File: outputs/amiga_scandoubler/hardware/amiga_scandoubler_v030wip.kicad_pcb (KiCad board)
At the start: 4 copper layers, 95 x 95 mm, 135 parts, among them J1 33DSMT1-E15SNCT, J2 33DSMT1-E15SNCT, J3 TYPE-C-31-M-12, J4 JTAG 2x05 2.54mm, U1 TVP7002PZP, U2 GW1N-LV4QN88C6/I5, U3 ADV7125KSTZ140, U4 SN74LVC2G17DBVR, U5 SN74LVC2G17DBVR, U6 SN74LVC1G17DBVR, U7 TPS62160DSGR, U8 TPS62160DSGR, U9 TPS62160DSGR, Y1 27MHz ECS-3225MVLC

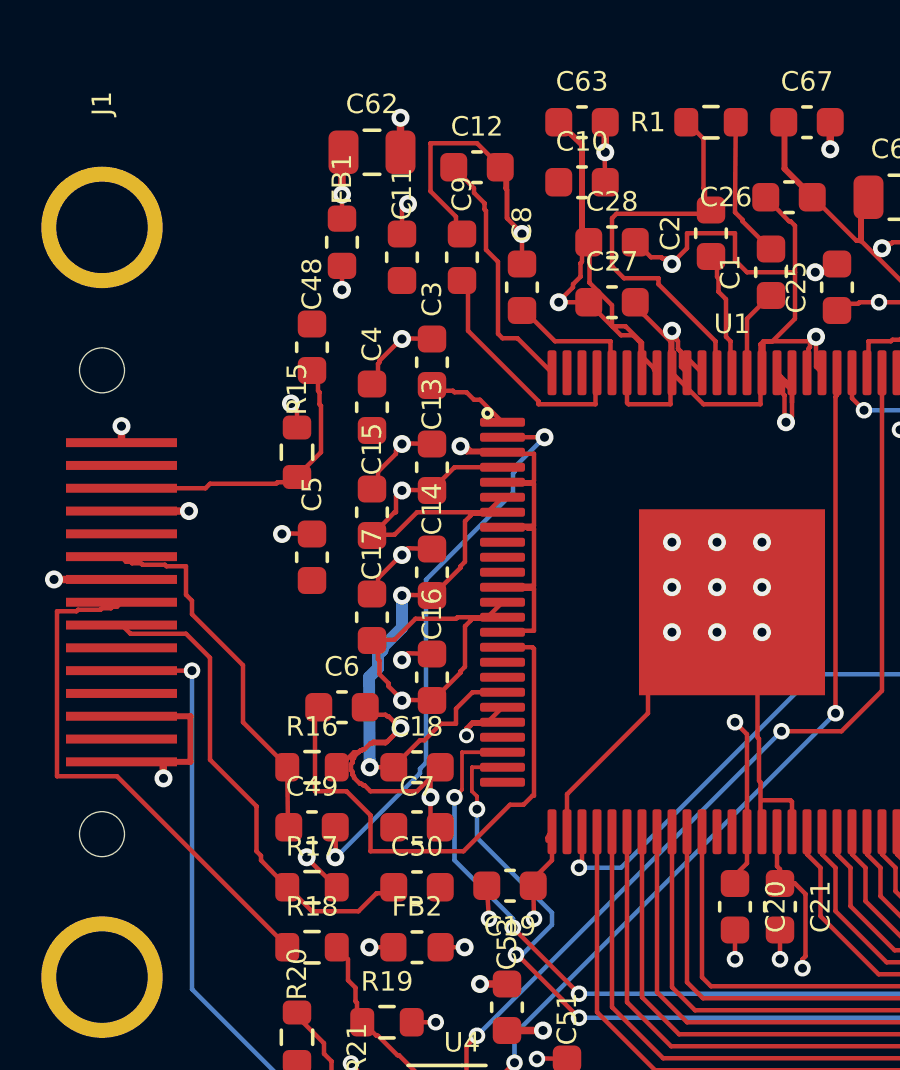
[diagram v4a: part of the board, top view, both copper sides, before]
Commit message: Issue 8: route the last analog inputs (board fully connected)
- Open the U1 input pins that other routing had walled in:
  - ADC_1V9A pin7 -> C14 and ADC_3V3A pin13/14 -> C16. The caps stay connected through their vias and In2.
  - The GIN_4, BIN_3 and GIN_1 routes.
  - The In2 ADC_1V9A and ADC_3V3A lines.
- RIN_1-3 escape through vias west of pins 9-11. The rest were routed with router7 and saved in p8_routes.json.
- The In2 3V3 zone now always removes isolated fill islands.
- DRC errors 0. Unconnected items 7 -> 0. 28 connectivity pairs checked. The power audit is unchanged.

Co-Authored-By: Claude Opus 5.5 <noreply@anthropic.com>
Claude-Session: https://claude.ai/code/session_019f929sAJ7LRnJRRFvA6g9F
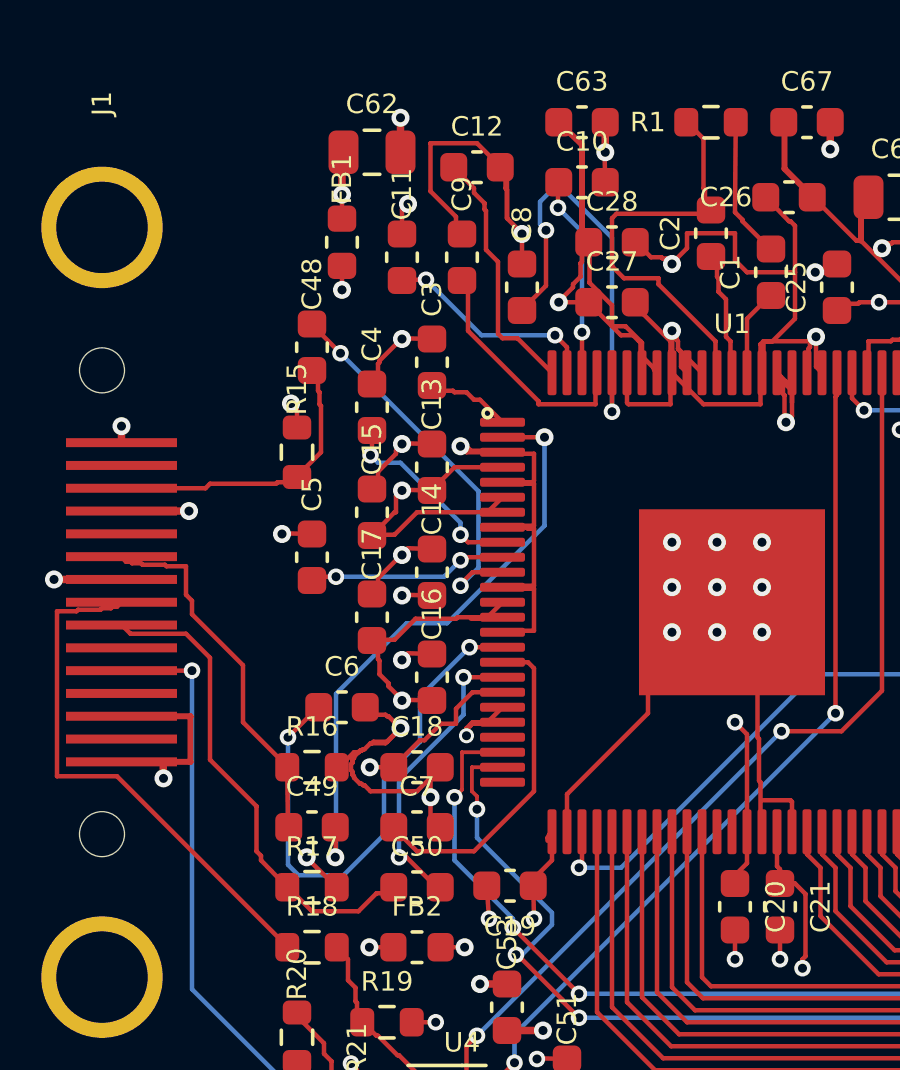
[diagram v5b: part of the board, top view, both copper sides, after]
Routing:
- net RIN_1: track 0.00 -> 12.1 mm, vias 0 -> 2
- net BIN_2: track 0.00 -> 11.1 mm
- net BIN_1: track 0.00 -> 9.95 mm, vias 0 -> 2
- net GIN_4: track 4.48 -> 14.3 mm, vias 0 -> 2
- net SOGIN_2: track 0.00 -> 7.28 mm, vias 0 -> 2
- net GIN_3: track 0.00 -> 6.68 mm, vias 0 -> 2
- net RIN_3: track 0.00 -> 5.96 mm, vias 0 -> 2
- net RIN_2: track 0.00 -> 5.91 mm, vias 0 -> 2
- net ADC_1V9A: track 63.0 -> 59.1 mm
- net ADC_3V3A: track 55.7 -> 53.6 mm
- net GIN_1: track 19.3 -> 20.1 mm
- net BIN_3: track 18.4 -> 18.1 mm, vias 0 -> 2

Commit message: Review fixes: decaps for U2 VCCO pins 12/23; move In2 lines off GIN_1
- #1: Add C70/C71 (100nF 0402) at 1.5 / 1.1 mm from U2 pins 12/23. Schematic, netlist and manifest updated; the schematic export matches the board on 591 nodes.
- #2: Re-draw the In2 ADC_3V3A/ADC_1V9A links so they cross GIN_1 instead of running under it (gap 4.9 -> 4.5 mm).
- #3: Stitching vias dropped. With In1 as the only GND plane they connect to nothing. Decaps near the REF_27M vias remain proposed.
- DRC errors 0, unconnected 0. The audit passes; its part/pad counts are updated to 137/596.

Co-Authored-By: Claude Opus 5.5 <noreply@anthropic.com>
Claude-Session: https://claude.ai/code/session_019f929sAJ7LRnJRRFvA6g9F
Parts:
- added C70: 100nF, C_0402_1005Metric, F.Cu at (57.0, 42.0)
- added C71: 100nF, C_0402_1005Metric, F.Cu at (54.8, 35.9)
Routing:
- net GND: track 370.1 -> 371.2 mm, vias 126 -> 127
- net 3V3: track 82.8 -> 83.5 mm
- net ADC_1V9A: track 59.1 -> 59.7 mm

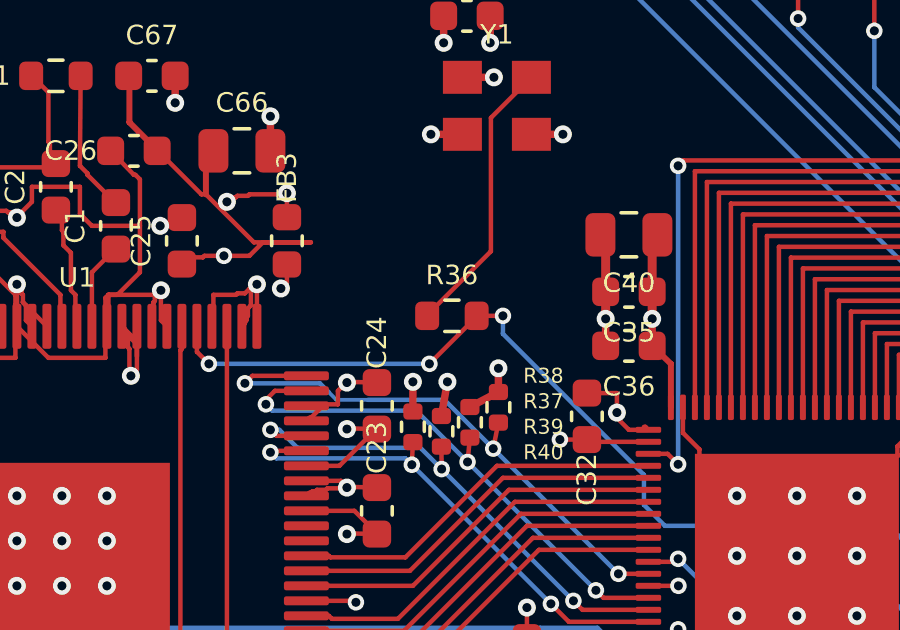
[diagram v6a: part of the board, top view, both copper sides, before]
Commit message: Add decaps C72/C73 next to the REF_27M layer-change vias
- Placements found by tools/capvia.py (0402, short stubs to new plane vias, no via-in-pad).
- Via-to-decap distance: 5.2 -> 1.6 mm and 4.3 -> 0.8 mm. The via under U1 (30.4,35.6) has no room and stays at 6.2 mm.
- Schematic (02_fpga), netlist and manifest updated; the schematic export matches the board on 595 nodes.
- DRC errors 0, unconnected 0. The audit passes with 139 parts / 600 pad nets.

Co-Authored-By: Claude Opus 5.5 <noreply@anthropic.com>
Claude-Session: https://claude.ai/code/session_019f929sAJ7LRnJRRFvA6g9F
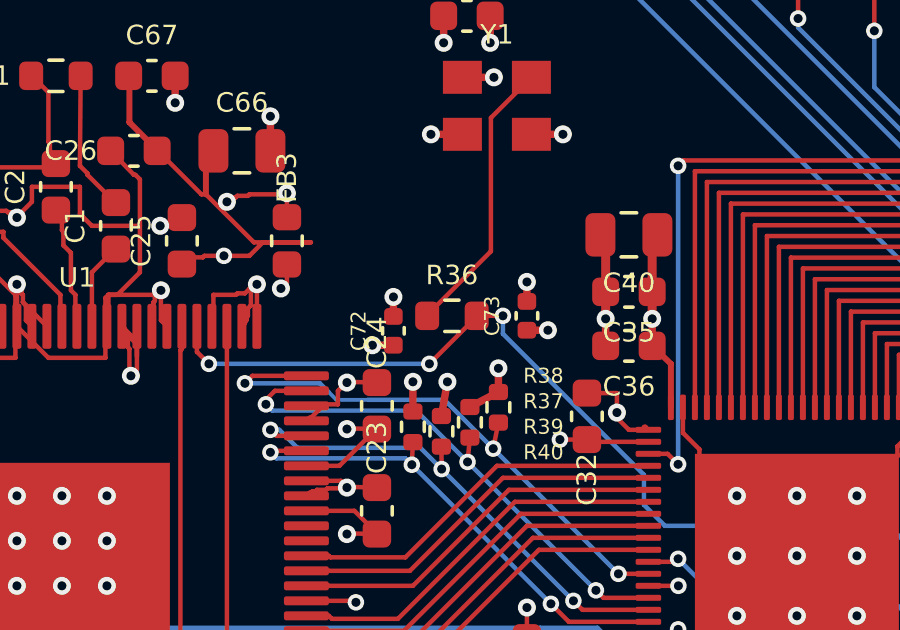
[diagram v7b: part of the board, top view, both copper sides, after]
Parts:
- added C72: 100nF, C_0402_1005Metric, F.Cu at (36.5, 34.5)
- added C73: 100nF, C_0402_1005Metric, F.Cu at (41.0, 34.0)
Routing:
- net 3V3: track 83.5 -> 84.9 mm, vias 39 -> 41
- net GND: track 371.2 -> 372.5 mm, vias 127 -> 129
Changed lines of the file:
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@@
     )
   )
+  (footprint "C_0402_1005Metric" (layer "F.Cu")
+    (at 36.55 34.5 90)
+    (descr "Capacitor SMD 0402 (1005 Metric), square (rectangular) end terminal, IPC_7351 nominal, (Body size source: IPC-SM-782 page 76, https://www.pcb-3d.com/wordpress/wp-content/uploads/ipc-sm-782a_amendment_1_and_2.pdf), generated with kicad-footprint-generator")
+    (tags "capacitor")
+    (property "LCSC" "")
+    (property "MPN" "100nF")
+    (attr smd)
+    (fp_text reference "C72" (at 0 -1.16 90) (layer "F.SilkS")
+        (effects (font (size 0.5 0.5) (thickness 0.08)))
+    )
+    (fp_text value "100nF" (at 0 1.16 90) (layer "F.Fab")
+        (effects (font (size 1 1) (thickness 0.15)))
+    )
+    (fp_text user "${REFERENCE}" (at 0 0 90) (layer "F.Fab")
+        (effects (font (size 0.25 0.25) (thickness 0.04)))
+    )
+    (fp_line (start -0.107836 -0.36) (end 0.107836 -0.36)
+      (stroke (width 0.12) (type solid)) (layer "F.SilkS"))
+    (fp_line (start -0.107836 0.36) (end 0.107836 0.36)
+      (stroke (width 0.12) (type solid)) (layer "F.SilkS"))
+    (fp_line (start -0.91 -0.46) (end 0.91 -0.46)
+      (stroke (width 0.05) (type solid)) (layer "F.CrtYd"))
+    (fp_line (start -0.91 0.46) (end -0.91 -0.46)
+      (stroke (width 0.05) (type solid)) (layer "F.CrtYd"))
+    (fp_line (start 0.91 -0.46) (end 0.91 0.46)
+      (stroke (width 0.05) (type solid)) (layer "F.CrtYd"))
+    (fp_line (start 0.91 0.46) (end -0.91 0.46)
+      (stroke (width 0.05) (type solid)) (layer "F.CrtYd"))
+    (fp_line (start -0.5 -0.25) (end 0.5 -0.25)
+      (stroke (width 0.1) (type solid)) (layer "F.Fab"))
+    (fp_line (start -0.5 0.25) (end -0.5 -0.25)
+      (stroke (width 0.1) (type solid)) (layer "F.Fab"))
+    (fp_line (start 0.5 -0.25) (end 0.5 0.25)
+      (stroke (width 0.1) (type solid)) (layer "F.Fab"))
+    (fp_line (start 0.5 0.25) (end -0.5 0.25)
+      (stroke (width 0.1) (type solid)) (layer "F.Fab"))
+    (pad "1" smd roundrect (at -0.48 0 90) (size 0.56 0.62) (layers "F.Cu" "F.Paste" "F.Mask") (roundrect_rratio 0.25)
+      (net 54 "3V3"))
+    (pad "2" smd roundrect (at 0.48 0 90) (size 0.56 0.62) (layers "F.Cu" "F.Paste" "F.Mask") (roundrect_rratio 0.25)
+      (net 43 "GND"))
+    (model "${KICAD6_3DMODEL_DIR}/Capacitor_SMD.3dshapes/C_0402_1005Metric.wrl"
+      (offset (xyz 0 0 0))
+      (scale (xyz 1 1 1))
+      (rotate (xyz 0 0 0))
+    )
+  )
   (footprint "Capacitor_SMD:C_0603_1608Metric" (layer "F.Cu")
     (at 25.3 29.7 90)
@@
     )
   )
+  (footprint "C_0402_1005Metric" (layer "F.Cu")
+    (at 41 34 90)
+    (descr "Capacitor SMD 0402 (1005 Metric), square (rectangular) end terminal, IPC_7351 nominal, (Body size source: IPC-SM-782 page 76, https://www.pcb-3d.com/wordpress/wp-content/uploads/ipc-sm-782a_amendment_1_and_2.pdf), generated with kicad-footprint-generator")
+    (tags "capacitor")
+    (property "LCSC" "")
+    (property "MPN" "100nF")
+    (attr smd)
+    (fp_text reference "C73" (at 0 -1.16 90) (layer "F.SilkS")
+        (effects (font (size 0.5 0.5) (thickness 0.08)))
+    )
+    (fp_text value "100nF" (at 0 1.16 90) (layer "F.Fab")
+        (effects (font (size 1 1) (thickness 0.15)))
+    )
+    (fp_text user "${REFERENCE}" (at 0 0 90) (layer "F.Fab")
+        (effects (font (size 0.25 0.25) (thickness 0.04)))
+    )
+    (fp_line (start -0.107836 -0.36) (end 0.107836 -0.36)
+      (stroke (width 0.12) (type solid)) (layer "F.SilkS"))
+    (fp_line (start -0.107836 0.36) (end 0.107836 0.36)
+      (stroke (width 0.12) (type solid)) (layer "F.SilkS"))
+    (fp_line (start -0.91 -0.46) (end 0.91 -0.46)
+      (stroke (width 0.05) (type solid)) (layer "F.CrtYd"))
+    (fp_line (start -0.91 0.46) (end -0.91 -0.46)
+      (stroke (width 0.05) (type solid)) (layer "F.CrtYd"))
+    (fp_line (start 0.91 -0.46) (end 0.91 0.46)
+      (stroke (width 0.05) (type solid)) (layer "F.CrtYd"))
+    (fp_line (start 0.91 0.46) (end -0.91 0.46)
+      (stroke (width 0.05) (type solid)) (layer "F.CrtYd"))
+    (fp_line (start -0.5 -0.25) (end 0.5 -0.25)
+      (stroke (width 0.1) (type solid)) (layer "F.Fab"))
+    (fp_line (start -0.5 0.25) (end -0.5 -0.25)
+      (stroke (width 0.1) (type solid)) (layer "F.Fab"))
+    (fp_line (start 0.5 -0.25) (end 0.5 0.25)
+      (stroke (width 0.1) (type solid)) (layer "F.Fab"))
+    (fp_line (start 0.5 0.25) (end -0.5 0.25)
+      (stroke (width 0.1) (type solid)) (layer "F.Fab"))
+    (pad "1" smd roundrect (at -0.48 0 90) (size 0.56 0.62) (layers "F.Cu" "F.Paste" "F.Mask") (roundrect_rratio 0.25)
+      (net 54 "3V3"))
+    (pad "2" smd roundrect (at 0.48 0 90) (size 0.56 0.62) (layers "F.Cu" "F.Paste" "F.Mask") (roundrect_rratio 0.25)
+      (net 43 "GND"))
+    (model "${KICAD6_3DMODEL_DIR}/Capacitor_SMD.3dshapes/C_0402_1005Metric.wrl"
+      (offset (xyz 0 0 0))
+      (scale (xyz 1 1 1))
+      (rotate (xyz 0 0 0))
+    )
+  )
   (footprint "Capacitor_SMD:C_0603_1608Metric" (layer "F.Cu")
     (at 20.5 58 90)
@@
   (segment (start 34 39.8) (end 34.3 39.8) (width 0.15) (layer "F.Cu") (net 43))
   (segment (start 76.6 40.95) (end 76.55 40.95) (width 0.15) (layer "F.Cu") (net 43))
+  (segment (start 36.55 34.02) (end 36.55 33.369999) (width 0.25) (layer "F.Cu") (net 43))
   (segment (start 68.85 44.75) (end 68.65 44.95) (width 0.15) (layer "F.Cu") (net 43))
   (segment (start 82.5 41.675) (end 82.4 41.55) (width 0.15) (layer "F.Cu") (net 43))
@@
   (segment (start 13.35 47.35) (end 13.35 47.25) (width 0.15) (layer "F.Cu") (net 43))
   (segment (start 78.1 40.8) (end 77.1 40.8) (width 0.15) (layer "F.Cu") (net 43))
+  (segment (start 41 33.52) (end 41 32.869999) (width 0.25) (layer "F.Cu") (net 43))
   (segment (start 31.65 34.15) (end 31.65 34.05) (width 0.15) (layer "F.Cu") (net 43))
   (segment (start 45.05 45.8) (end 46.4 45.8) (width 0.15) (layer "F.Cu") (net 43))
@@
   (via (at 46.675 77) (size 0.6) (drill 0.3) (layers "F.Cu" "B.Cu") (net 43))
   (via (at 15 36.725) (size 0.6) (drill 0.3) (layers "F.Cu" "B.Cu") (net 43))
+  (via (at 36.55 33.369999) (size 0.6) (drill 0.3) (layers "F.Cu" "B.Cu") (net 43))
   (via (at 24 30.725) (size 0.6) (drill 0.3) (layers "F.Cu" "B.Cu") (net 43))
   (via (at 80.5 40.725) (size 0.6) (drill 0.3) (layers "F.Cu" "B.Cu") (net 43))
@@
   (via (at 68.6375 44.95) (size 0.6) (drill 0.3) (layers "F.Cu" "B.Cu") (net 43))
   (via (at 29.275 26.9) (size 0.6) (drill 0.3) (layers "F.Cu" "B.Cu") (net 43))
+  (via (at 41 32.869999) (size 0.6) (drill 0.3) (layers "F.Cu" "B.Cu") (net 43))
   (via (at 15 40.425) (size 0.6) (drill 0.3) (layers "F.Cu" "B.Cu") (net 43))
   (via (at 36.2 46.9) (size 0.55) (drill 0.3) (layers "F.Cu" "B.Cu") (net 43))
@@
   (segment (start 56.2 42.05) (end 55.95 42) (width 0.25) (layer "F.Cu") (net 54))
   (segment (start 33.65 47) (end 34.7 47) (width 0.15) (layer "F.Cu") (net 54))
+  (segment (start 41 34.48) (end 41.7 34.48) (width 0.25) (layer "F.Cu") (net 54))
   (segment (start 75.1 50.5) (end 74.9 50.3) (width 0.15) (layer "F.Cu") (net 54))
+  (segment (start 36.55 34.98) (end 35.85 34.98) (width 0.25) (layer "F.Cu") (net 54))
   (segment (start 35 41.25) (end 35 41.275) (width 0.15) (layer "F.Cu") (net 54))
   (segment (start 75.225 54) (end 75.225 54.95) (width 0.25) (layer "F.Cu") (net 54))
@@
   (via (at 40.05 35.75) (size 0.6) (drill 0.3) (layers "F.Cu" "B.Cu") (net 54))
   (via (at 13.3 57.375) (size 0.55) (drill 0.3) (layers "F.Cu" "B.Cu") (net 54))
+  (via (at 41.7 34.48) (size 0.6) (drill 0.3) (layers "F.Cu" "B.Cu") (net 54))
   (via (at 78.3 57.825) (size 0.6) (drill 0.3) (layers "F.Cu" "B.Cu") (net 54))
   (via (at 41 43.725) (size 0.6) (drill 0.3) (layers "F.Cu" "B.Cu") (net 54))
@@
   (via (at 37.2 36.2) (size 0.6) (drill 0.3) (layers "F.Cu" "B.Cu") (net 54))
   (via (at 38.825 76.6) (size 0.6) (drill 0.3) (layers "F.Cu" "B.Cu") (net 54))
+  (via (at 35.85 34.98) (size 0.6) (drill 0.3) (layers "F.Cu" "B.Cu") (net 54))
   (via (at 39.9 14.825) (size 0.6) (drill 0.3) (layers "F.Cu" "B.Cu") (net 54))
   (via (at 46.04 45.2) (size 0.55) (drill 0.3) (layers "F.Cu" "B.Cu") (net 54))

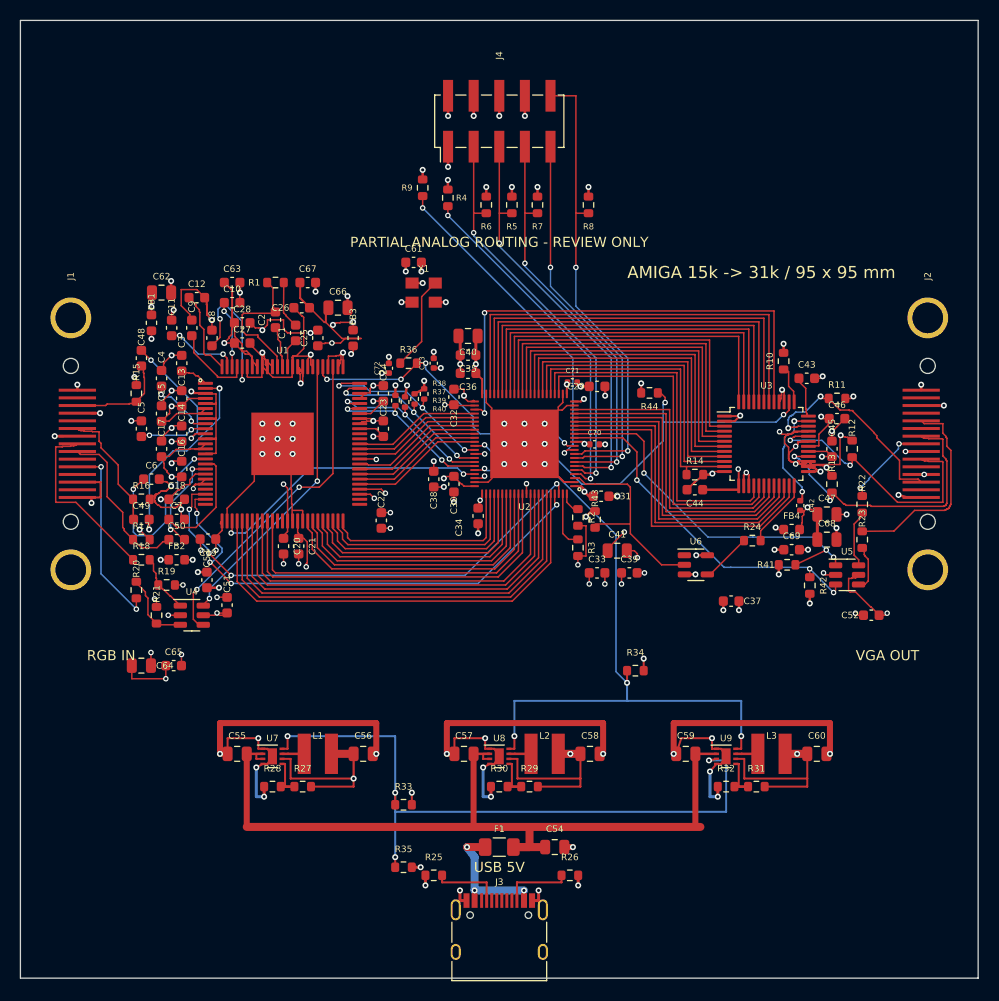
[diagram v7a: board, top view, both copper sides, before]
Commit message: Issue 10: silkscreen clean-up, fab outputs and bitstreams
- Silkscreen:
  - All 139 reference designators set to 0.8/0.15 mm and auto-placed clear of pad openings, silk, texts and the board edge; none hidden.
  - The stale review banner is replaced by the revision text, and the U1/U2 pin-1 markers are moved off their pads.
  - Silk warnings drop from ~220 to 2 (the J3 outline at the board edge).
- fab/v030wip: Gerbers, drills (PTH/NPTH), position file, JLC BOM/CPL, parts-to-select list, gerbv preview.
  - Drill hits match the board (303 PTH / 6 NPTH).
- Bitstreams for H_SAMPLES 1816/2048 packed with apycula. They are not verified on hardware.
- DRC errors 0, unconnected 0. The audit passes. Nothing was uploaded or ordered.

Co-Authored-By: Claude Opus 5.5 <noreply@anthropic.com>
Claude-Session: https://claude.ai/code/session_019f929sAJ7LRnJRRFvA6g9F
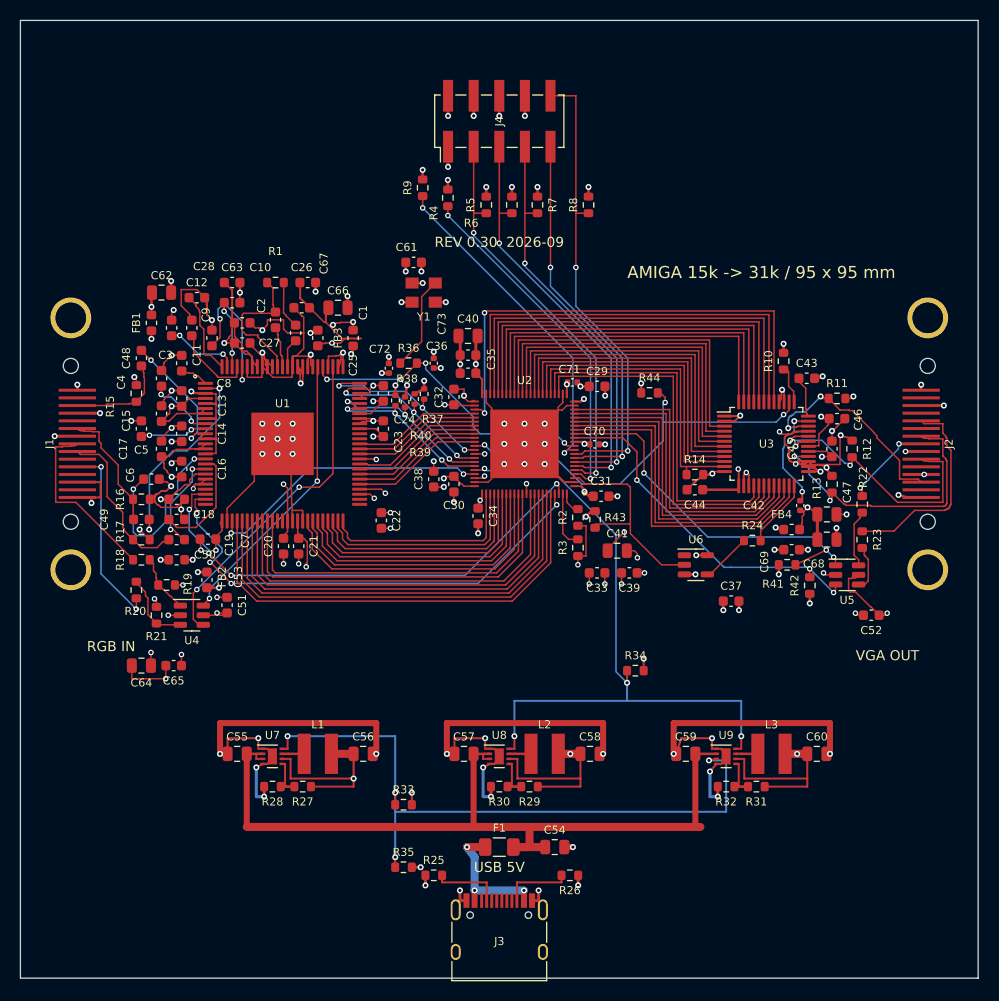
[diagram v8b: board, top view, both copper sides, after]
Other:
- board text added: "REV 0.30 2026-09"
- board text removed: "PARTIAL ANALOG ROUTING - REVIEW ONLY"
